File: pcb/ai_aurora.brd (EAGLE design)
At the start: 73.8 x 73.8 mm, 1 part

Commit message: schematic done
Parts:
- added BAT1, BAT2: (no value), Ai_Electromechanical:BATTERY-AAA
- added C1, C2, C3: (no value), Ai_Passives:CAP-025X050
- added D1: (no value), Ai_DiscreteSemis:TH-1N914
- added IC1: ATTINY85-DIP, Ai_IC:DIL08
- added J1: 1X02ST, Ai_Connectors:1X02-ST
- added J2: 2X03, Ai_Connectors:2X03
- added LDR: LDR-PTH, Ai_Sensors:LDR
- added Q3: (no value), Ai_DiscreteSemis:TO-92-NPN
- added Q4: (no value), Ai_DiscreteSemis:TO-92-PNP
- added R2: 1K, Ai_Passives:RES-AXIAL-0.4
- added R5: 100K, Ai_Passives:RES-AXIAL-0.4
- added R6: 10K, Ai_Passives:RES-AXIAL-0.4
- added R7: 1M, Ai_Passives:RES-AXIAL-0.4
- added U$4, U$5: LED-PL9823-F8, Ai_LED:LED-RGB-PTH
- R1: value LDR-PTH -> 1K; device Ai_Sensors:LDR -> Ai_Passives:RES-AXIAL-0.4
- moved R1 45.8 mm to (11.4, -30.5)
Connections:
- new net +: C1.1, C2.1, IC1.8, J2.2, Q4.1, R2.P$2
- new net -: C1.2, C2.2, IC1.4, J2.6, R1.P$2, R7.P$1
- new net DI: IC1.2, U$4.4
- new net DO: U$5.1
- new net GND: C3.2, J1.2, LDR.1, Q3.1, R1.P$1
- new net MISO: IC1.6, J2.1
- new net MOSI: IC1.5, J2.4
- new net N$1: BAT1.PWR@1, BAT1.PWR@2, BAT2.GND@1, BAT2.GND@2
- new net N$10: LDR.2, Q3.2, R5.P$1, R7.P$2
- new net N$12: Q3.3, R6.P$2
- new net N$13: Q4.2, R6.P$1
- new net N$2: D1.A, J1.1
- new net N$4: U$4.1, U$5.4
- new net N$6: U$4.3, U$5.3
- new net N$7: U$4.2, U$5.2
- new net RST: IC1.1, J2.5, R2.P$1
- new net SCK: IC1.7, J2.3
- new net VBAT: BAT2.PWR@1, BAT2.PWR@2, Q4.3, R5.P$2
- new net VIN: BAT1.GND@1, BAT1.GND@2, C3.1, D1.C
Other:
- board text added: "+"

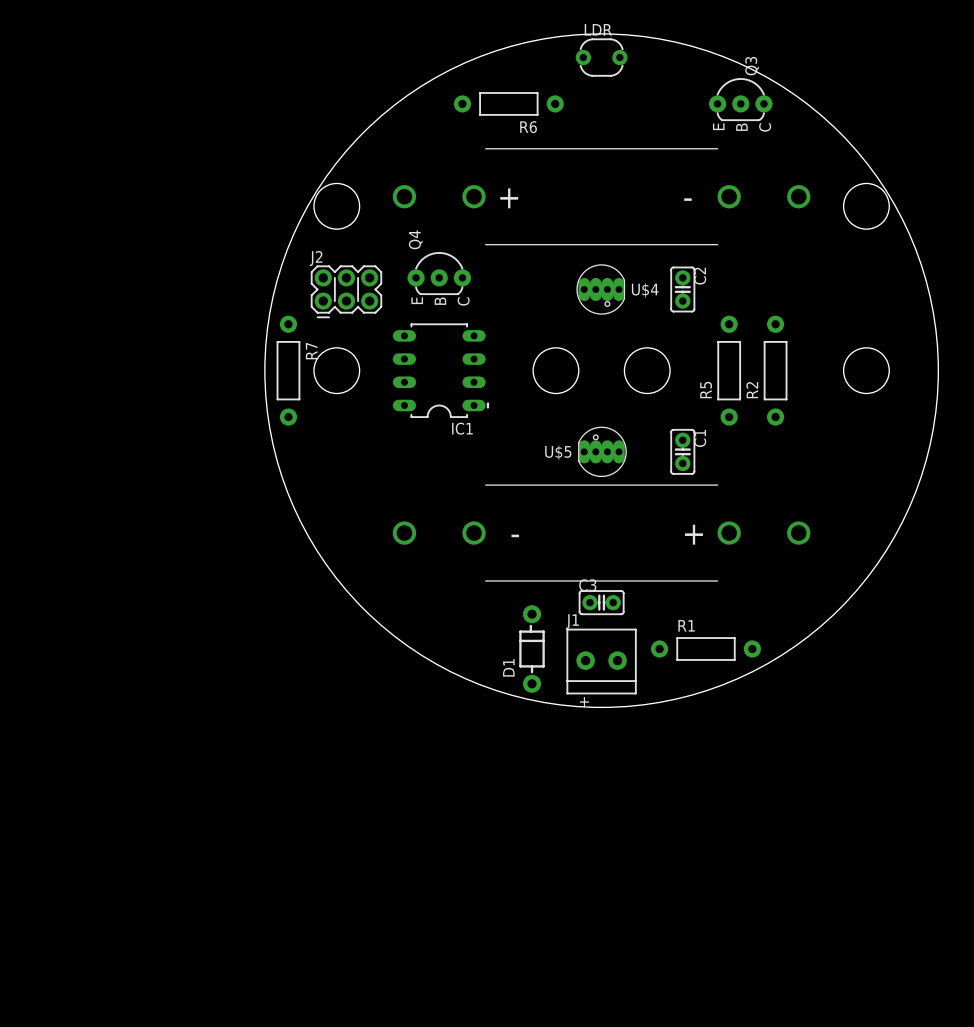
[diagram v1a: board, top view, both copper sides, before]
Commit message: some fitting issues remain
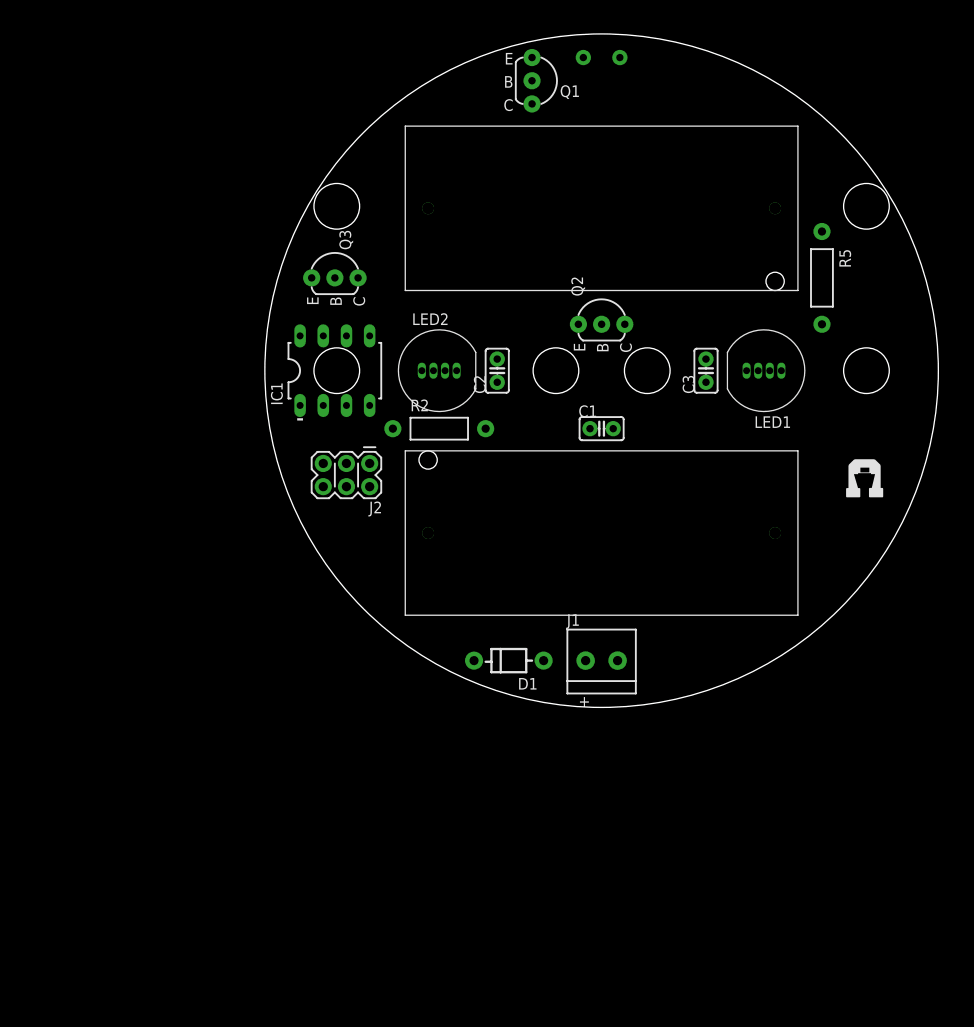
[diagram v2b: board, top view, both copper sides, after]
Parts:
- removed Q4: (no value), Ai_DiscreteSemis:TO-92-PNP
- removed R1: 1K, Ai_Passives:RES-AXIAL-0.4
- removed R6: 10K, Ai_Passives:RES-AXIAL-0.4
- removed R7: 1M, Ai_Passives:RES-AXIAL-0.4
- added LED1, LED2: LED-PL9823-F8, Ai_LED:LED-PL9823-F8
- added Q1: (no value), Ai_DiscreteSemis:TO-92-NPN
- added Q2: (no value), Ai_DiscreteSemis:TO-92-PNP
- BAT1, BAT2: device Ai_Electromechanical:BATTERY-AAA -> Ai_Electromechanical:BATTERY-CR123A
- U$4, U$5: value LED-PL9823-F8 -> AI-LOGOM; device Ai_LED:LED-RGB-PTH -> Ai_Miscellany:AI-LOGO-M
- moved Q3 48.4 mm to (-29.2, 10.2)
- moved R2 37.4 mm to (-17.8, -6.35), turned to 0 degrees
- moved U$4 35.1 mm to (26.7, -14.0)
- moved U$5 31.4 mm to (31.0, -14.0), flipped to the bottom, turned to 0 degrees
- moved C3 27.9 mm to (11.4, 0.00), turned to 90 degrees
- moved C2 22.2 mm to (-11.4, 0.00), turned to 90 degrees
- moved J2 20.3 mm to (-27.9, -11.4), turned to 180 degrees
- moved R5 14.4 mm to (24.1, 10.2), turned to 270 degrees
- moved IC1 11.4 mm to (-29.2, 0.00), turned to 0 degrees
- moved C1 9.25 mm to (0.00, -6.35), turned to 0 degrees
- moved D1 2.84 mm to (-10.2, -31.8), turned to 180 degrees
- moved BAT1 1.27 mm to (0.00, 17.8), turned to 270 degrees
- turned BAT2 to 90 degrees
- flipped LDR to the bottom
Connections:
- removed net -: C1.2, C2.2, IC1.4, J2.6, R1.P$2, R7.P$1
- removed net N$12: Q3.3, R6.P$2
- removed net N$6: U$4.3, U$5.3
- removed net N$7: U$4.2, U$5.2
- net +: now also LED1.2, LED2.2, Q2.1, Q3.1, Q3.2; no longer Q4.1
- net DI: now also LED1.1; no longer U$4.4
- net DO: now also LED2.4; no longer U$5.1
- net GND: now also C1.2, C2.2, IC1.4, J2.6, LED1.3, LED2.3, Q1.1; no longer Q3.1, R1.P$1
- net N$1: now also BAT1.+, BAT2.-; no longer BAT1.PWR@1, BAT1.PWR@2, BAT2.GND@1, BAT2.GND@2
- net N$10: now also Q1.2; no longer Q3.2, R7.P$2
- net N$13: now also Q1.3, Q2.2; no longer Q4.2, R6.P$1
- net N$4: now also LED1.4, LED2.1; no longer U$4.1, U$5.4
- net VBAT: now also BAT2.+, Q2.3, Q3.3; no longer BAT2.PWR@1, BAT2.PWR@2, Q4.3
- net VIN: now also BAT1.-; no longer BAT1.GND@1, BAT1.GND@2

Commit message: updating firmware and pcb
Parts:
- removed Q2: (no value), Ai_DiscreteSemis:TO-92-PNP
- removed Q3: (no value), Ai_DiscreteSemis:TO-92-NPN
- added JP1, JP2: 1X02-PJ, Ai_Connectors:1X02
- added R1: 10K, Ai_Passives:RES-AXIAL-0.4
- added S1, S2: SW-SPSTTH06X06, Ai_Electromechanical:SW-SPST-TH06X06
- added VR1: 1M, Ai_Passives:POT-05X05
- C3: value (none) -> 4.7uF; device Ai_Passives:CAP-025X050 -> Ai_Passives:CAP-POL-025X50
- Q1: value (none) -> FQP30N06L; device Ai_DiscreteSemis:TO-92-NPN -> Ai_DiscreteSemis:TO-220
- R2: value 1K -> 10K
- moved Q1 99.4 mm to (-52.1, -57.1), turned to 0 degrees
- moved R2 69.4 mm to (-57.1, -63.5)
- moved C3 1.27 mm to (11.4, 1.27)
- renumbered LDR to LDR1
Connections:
- net MOSI renamed MOSI/SET
- removed net MISO: IC1.6, J2.1
- removed net N$10: LDR1.2, Q1.2, R5.P$1
- removed net N$13: Q1.3, Q2.2
- removed net SCK: IC1.7, J2.3
- new net -: C1.2, C2.2, LED1.3, LED2.3, Q1.2
- new net LED_EN: IC1.3, Q1.1
- new net MISO/LDR: IC1.6, J2.1, JP1.1
- new net N$3: R1.P$2, S1.B@1
- new net N$5: R2.P$2, S2.A@1
- new net N$6: R5.P$2, VR1.2
- new net N$7: JP1.2, LDR1.2, R5.P$1
- new net SCK/BATT: IC1.7, J2.3, JP2.1
- net +: no longer IC1.8, J2.2, Q2.1, Q3.1, Q3.2, R2.P$2
- net GND: now also C3.C, Q1.3, R1.P$1, R2.P$1; no longer C1.2, C2.2, C3.2, LED1.3, LED2.3, Q1.1
- net RST: now also S1.A@1; no longer R2.P$1
- net VBAT: now also IC1.8, J2.2, JP2.2, VR1.3; no longer Q2.3, Q3.3, R5.P$2
- net VIN: now also C3.A; no longer C3.1

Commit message: updating
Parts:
- removed R5: 100K, Ai_Passives:RES-AXIAL-0.4
- added R3: 10K, Ai_Passives:RES-AXIAL-0.4
- added R4: 100K, Ai_Passives:RES-AXIAL-0.4
- R2: value 10K -> 100K
- moved R2 109.7 mm to (24.1, 10.2), turned to 270 degrees
- renumbered C3 to C11
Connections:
- net GND: now also R3.P$1, R4.P$1; no longer R2.P$1
- net LED_EN: now also R4.P$2
- net N$5: now also R3.P$2; no longer R2.P$2
- net N$6: now also R2.P$2; no longer R5.P$2
- net N$7: now also R2.P$1; no longer R5.P$1
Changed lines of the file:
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@@
 <element name="IC1" library="Ai_IC" package="DIL08" value="ATTINY85-DIP" x="-29.21" y="0"/>
 <element name="LDR1" library="Ai_Sensors" package="LDR" value="LDR-PTH" x="0" y="34.29" rot="MR0"/>
-<element name="R5" library="Ai_Passives" package="RES-AXIAL-0.4" value="100K" x="24.13" y="10.16" rot="R270"/>
+<element name="R2" library="Ai_Passives" package="RES-AXIAL-0.4" value="100K" x="24.13" y="10.16" rot="R270"/>
 <element name="BAT1" library="Ai_Electromechanical" package="BATTERY-CR123A" value="" x="0" y="17.78" rot="R270"/>
 <element name="BAT2" library="Ai_Electromechanical" package="BATTERY-CR123A" value="" x="0" y="-17.78" rot="R90"/>
@@
 <element name="J1" library="Ai_Connectors" package="1X02-ST" value="1X02ST" x="0" y="-31.75"/>
 <element name="J2" library="Ai_Connectors" package="2X03" value="2X03" x="-27.94" y="-11.43" rot="R180"/>
-<element name="C3" library="Ai_Passives" package="CAP-POL-025X50" value="4.7uF" x="11.43" y="1.27" rot="R90"/>
+<element name="C11" library="Ai_Passives" package="CAP-POL-025X50" value="4.7uF" x="11.43" y="1.27" rot="R90"/>
 <element name="LED1" library="Ai_LED" package="LED-PL9823-F8" value="LED-PL9823-F8" x="17.78" y="0" rot="R180"/>
 <element name="LED2" library="Ai_LED" package="LED-PL9823-F8" value="LED-PL9823-F8" x="-17.78" y="0"/>
@@
 <element name="Q1" library="Ai_DiscreteSemis" package="TO-220" value="FQP30N06L" x="-52.07" y="-57.15"/>
 <element name="S2" library="Ai_Electromechanical" package="SW-SPST-TH06X06" value="SW-SPSTTH06X06" x="-59.69" y="-54.61"/>
-<element name="R2" library="Ai_Passives" package="RES-AXIAL-0.4" value="10K" x="-57.15" y="-63.5"/>
+<element name="R3" library="Ai_Passives" package="RES-AXIAL-0.4" value="10K" x="-57.15" y="-63.5"/>
+<element name="R4" library="Ai_Passives" package="RES-AXIAL-0.4" value="100K" x="-57.15" y="-68.58"/>
 </elements>
 <signals>
 <signal name="GND" airwireshidden="yes">
 <contactref element="LDR1" pad="1"/>
-<contactref element="C3" pad="C"/>
+<contactref element="C11" pad="C"/>
 <contactref element="J1" pad="2"/>
 <contactref element="IC1" pad="4"/>
@@
 <contactref element="R1" pad="P$1"/>
 <contactref element="Q1" pad="3"/>
-<contactref element="R2" pad="P$1"/>
+<contactref element="R3" pad="P$1"/>
+<contactref element="R4" pad="P$1"/>
+<wire x1="-62.23" y1="-63.5" x2="-62.23" y2="-68.58" width="0" layer="19" extent="1-1"/>
 <wire x1="-49.53" y1="-57.15" x2="-62.23" y2="-63.5" width="0" layer="19" extent="1-1"/>
 <wire x1="-35.56" y1="-41.91" x2="-49.53" y2="-57.15" width="0" layer="19" extent="1-1"/>
@@
 <contactref element="D1" pad="C"/>
 <contactref element="BAT1" pad="-"/>
-<contactref element="C3" pad="A"/>
+<contactref element="C11" pad="A"/>
 <wire x1="11.43" y1="2.54" x2="-13.97" y2="-31.75" width="0" layer="19" extent="1-1"/>
 <wire x1="-19" y1="17.78" x2="11.43" y2="2.54" width="0" layer="19" extent="1-1"/>
@@
 <contactref element="IC1" pad="3"/>
 <contactref element="Q1" pad="1"/>
+<contactref element="R4" pad="P$2"/>
+<wire x1="-54.61" y1="-57.15" x2="-52.07" y2="-68.58" width="0" layer="19" extent="1-1"/>
 <wire x1="-27.94" y1="-3.81" x2="-54.61" y2="-57.15" width="0" layer="19" extent="1-1"/>
 </signal>
 <signal name="N$6">
-<contactref element="R5" pad="P$2"/>
+<contactref element="R2" pad="P$2"/>
 <contactref element="VR1" pad="2"/>
 <wire x1="24.13" y1="5.08" x2="-50.8" y2="-36.83" width="0" layer="19" extent="1-1"/>
@@
 <signal name="N$7">
 <contactref element="LDR1" pad="2"/>
-<contactref element="R5" pad="P$1"/>
+<contactref element="R2" pad="P$1"/>
 <contactref element="JP1" pad="2"/>
 <wire x1="-2" y1="34.29" x2="-49.53" y2="-46.99" width="0" layer="19" extent="1-1"/>
@@
 </signal>
 <signal name="N$5">
-<contactref element="R2" pad="P$2"/>
+<contactref element="R3" pad="P$2"/>
 <contactref element="S2" pad="A@1"/>
 <wire x1="-52.07" y1="-63.5" x2="-62.9412" y2="-56.8706" width="0" layer="19" extent="1-1"/>

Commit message: gerbers
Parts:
- removed J1: 1X02ST, Ai_Connectors:1X02-ST
- removed J2: 2X03, Ai_Connectors:2X03
- removed S1, S2: SW-SPSTTH06X06, Ai_Electromechanical:SW-SPST-TH06X06
- added ISP: 2X03, Ai_Connectors:2X03
- added M2, M3, PANEL+, PANEL-: 1X01-TERM-PANEL, Ai_Connectors:1X01-PANEL
- added RESET, SET: SW-SPSTTH06X06, Ai_Electromechanical:SW-SPST-TH06X06
- added SOLAR-IN: 1X02ST, Ai_Connectors:1X02-ST
- moved R3 89.6 mm to (-8.38, 11.7), turned to 270 degrees
- moved R4 87.3 mm to (8.38, -10.9), turned to 270 degrees
- moved VR1 74.8 mm to (-16.3, 26.9)
- moved Q1 70.1 mm to (0.00, -10.2), turned to 180 degrees
- moved JP2 48.7 mm to (-7.24, -30.2), turned to 90 degrees
- moved D1 47.1 mm to (31.8, -10.2), turned to 270 degrees
- moved LED1 44.5 mm to (-17.8, -26.7)
- moved LED2 44.5 mm to (17.8, 26.7)
- moved IC1 43.3 mm to (1.27, -30.7), turned to 270 degrees
- moved JP1 43.3 mm to (-10.9, -30.2), turned to 90 degrees
- moved C2 42.7 mm to (23.6, 24.4)
- moved U$5 40.9 mm to (0.31, 13.1), turned to 270 degrees
- moved R1 38.1 mm to (-8.38, -10.9), turned to 270 degrees
- moved R2 37.1 mm to (-8.13, 28.4), turned to 90 degrees
- moved U$4 34.8 mm to (0.31, 8.77), turned to 90 degrees
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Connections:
- removed net N$2: D1.A, J1.1
- new net VPANEL: D1.A, PANEL+.1, SOLAR-IN.1
- net GND: now also ISP.6, PANEL-.1, SOLAR-IN.2; no longer J1.2, J2.6
- net MISO/LDR: now also ISP.1; no longer J2.1
- net MOSI/SET: now also ISP.4, SET.B@1; no longer J2.4
- net N$3: now also RESET.B@1; no longer S1.B@1
- net N$5: now also SET.A@1; no longer S2.A@1
- net RST: now also ISP.5, RESET.A@1; no longer J2.5, S1.A@1
- net SCK/BATT: now also ISP.3; no longer J2.3
- net VBAT: now also ISP.2; no longer J2.2
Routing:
- net VBAT: track 0.00 -> 110.9 mm, vias 0 -> 1
- net N$7: track 0.00 -> 95.9 mm
- net +: track 0.00 -> 95.8 mm, vias 0 -> 1
- net N$4: track 0.00 -> 93.4 mm
- net -: track 0.00 -> 93.4 mm
- net VIN: track 0.00 -> 64.3 mm
- net LED_EN: track 0.00 -> 60.9 mm
- net VPANEL: track 0.00 -> 48.1 mm
- net N$1: track 0.00 -> 39.4 mm
- net MOSI/SET: track 0.00 -> 39.3 mm
- net RST: track 0.00 -> 28.5 mm
- net MISO/LDR: track 0.00 -> 28.3 mm
- net N$5: track 0.00 -> 27.9 mm
- net SCK/BATT: track 0.00 -> 22.0 mm
- net DI: track 0.00 -> 15.4 mm
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- added copper zone on layer 1, net GND
- added copper zone on layer 16, net GND
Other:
- outline, holes or cut-outs redrawn
- board text added: "AURORA"
- board text added: "Pasadena, CA"
- board text added: "SENSITIVITY"
- board text added: "The Smart Sun Jar"
- board text added: "v1.0"
- board text added: "www.acrobotic.com"

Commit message: updated libraries
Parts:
- BAT1, BAT2: value (none) -> CR123A
- C1, C2: value (none) -> 0.1uF
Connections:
- removed net +: C1.1, C2.1, LED1.2, LED2.2
- net VBAT: now also C1.1, C2.1, LED1.2, LED2.2
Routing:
- net VBAT: track 110.9 -> 208.3 mm, vias 1 -> 2
- net +: track 95.8 -> 0.00 mm, vias 1 -> 0
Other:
- outline, holes or cut-outs redrawn
- board text added: "-"
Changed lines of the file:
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@@
 <setting verticaltext="up"/>
 </settings>
-<grid distance="10" unitdist="mil" unit="mil" style="lines" multiple="1" display="yes" altdistance="0.025" altunitdist="inch" altunit="inch"/>
+<grid distance="1" unitdist="mil" unit="mil" style="lines" multiple="1" display="yes" altdistance="0.025" altunitdist="inch" altunit="inch"/>
 <layers>
 <layer number="1" name="Top" color="4" fill="1" visible="yes" active="yes"/>
@@
 <layer number="223" name="223bmp" color="24" fill="1" visible="no" active="no"/>
 <layer number="224" name="224bmp" color="25" fill="1" visible="no" active="no"/>
+<layer number="225" name="225bmp" color="7" fill="1" visible="no" active="yes"/>
+<layer number="226" name="226bmp" color="7" fill="1" visible="no" active="yes"/>
+<layer number="227" name="227bmp" color="7" fill="1" visible="no" active="yes"/>
+<layer number="228" name="228bmp" color="7" fill="1" visible="no" active="yes"/>
+<layer number="230" name="230bmp" color="7" fill="1" visible="no" active="yes"/>
 <layer number="248" name="Housing" color="7" fill="1" visible="yes" active="yes"/>
 <layer number="249" name="Edge" color="7" fill="1" visible="yes" active="yes"/>
@@
 <plain>
 <circle x="0" y="0" radius="36.875" width="0.0254" layer="20"/>
-<circle x="30.27" y="19.905" radius="2.5" width="0.0254" layer="20"/>
-<text x="36.83" y="-2.54" size="1.27" layer="21" font="vector" ratio="10" rot="R90">+</text>
+<text x="31.75" y="-2.286" size="1.778" layer="21" font="vector" ratio="10" rot="R90">+</text>
 <text x="-16.256" y="23.114" size="1.016" layer="21" font="vector" ratio="10" align="center">SENSITIVITY</text>
-<text x="2.09" y="13.845" size="1.016" layer="21" font="vector" ratio="10" rot="R90" align="center">Pasadena, CA</text>
-<text x="3.868" y="15.369" size="1.016" layer="21" font="vector" ratio="10" rot="R90" align="center">www.acrobotic.com</text>
-<text x="1.836" y="13.845" size="1.016" layer="22" font="vector" ratio="10" rot="SMR270" align="center">Pasadena, CA</text>
-<text x="3.614" y="15.369" size="1.016" layer="22" font="vector" ratio="10" rot="SMR270" align="center">www.acrobotic.com</text>
+<text x="2.1408" y="14.2006" size="1.016" layer="21" font="vector" ratio="10" rot="R90" align="center">Pasadena, CA</text>
+<text x="3.8426" y="15.8008" size="1.016" layer="21" font="vector" ratio="10" rot="R90" align="center">www.acrobotic.com</text>
+<text x="2.1408" y="13.9466" size="1.016" layer="22" font="vector" ratio="10" rot="SMR270" align="center">Pasadena, CA</text>
+<text x="3.7918" y="15.5722" size="1.016" layer="22" font="vector" ratio="10" rot="SMR270" align="center">www.acrobotic.com</text>
 <text x="-29.718" y="-18.288" size="1.016" layer="21" font="vector" ratio="10" rot="R90" align="center">v1.0</text>
 <text x="-33.274" y="0" size="2.54" layer="21" font="vector" ratio="10" rot="R90" align="center">AURORA</text>
 <text x="-29.972" y="0" size="1.778" layer="21" font="vector" ratio="10" rot="R90" align="center">The Smart Sun Jar</text>
+<text x="31.75" y="1.143" size="1.778" layer="21" font="vector" ratio="10" rot="R90">-</text>
 </plain>
 <attributes>
@@
 <attribute name="NAME" x="-9.779" y="31.115" size="1.27" layer="25" font="vector" ratio="10" rot="R90"/>
 </element>
-<element name="BAT1" library="Ai_Electromechanical" package="BATTERY-CR123A" value="" x="-19.05" y="0"/>
-<element name="BAT2" library="Ai_Electromechanical" package="BATTERY-CR123A" value="" x="19.05" y="0" rot="R180"/>
-<element name="C1" library="Ai_Passives" package="CAP-025X050" value="" x="-23.876" y="-24.384" rot="R270"/>
-<element name="C2" library="Ai_Passives" package="CAP-025X050" value="" x="23.622" y="24.384" rot="R90"/>
+<element name="BAT1" library="Ai_Electromechanical" package="BATTERY-CR123A" value="CR123A" x="-19.05" y="0"/>
+<element name="BAT2" library="Ai_Electromechanical" package="BATTERY-CR123A" value="CR123A" x="19.05" y="0" rot="R180"/>
+<element name="C1" library="Ai_Passives" package="CAP-025X050" value="0.1uF" x="-23.876" y="-24.384" rot="R270"/>
+<element name="C2" library="Ai_Passives" package="CAP-025X050" value="0.1uF" x="23.622" y="24.384" rot="R90"/>
 <element name="D1" library="Ai_DiscreteSemis" package="TH-1N914" value="" x="31.75" y="-10.16" rot="R270"/>
 <element name="SOLAR-IN" library="Ai_Connectors" package="1X02-ST" value="1X02ST" x="35.036" y="0" smashed="yes" rot="R90">
@@
 <wire x1="17.526" y1="-7.366" x2="19.05" y2="-8.89" width="0.4064" layer="1"/>
 <wire x1="19.05" y1="-8.89" x2="19.05" y2="-19" width="0.4064" layer="1"/>
-</signal>
-<signal name="+">
 <contactref element="C1" pad="1"/>
 <contactref element="C2" pad="1"/>
@@
 <wire x1="-17.272" y1="-22.86" x2="-17.145" y2="-22.733" width="0.4064" layer="1"/>
 <via x="-17.145" y="-22.733" extent="1-16" drill="0.508"/>
+<wire x1="0" y1="-6.35" x2="-0.508" y2="-6.35" width="0.4064" layer="16"/>
+<wire x1="-0.508" y1="-6.35" x2="-1.27" y2="-5.588" width="0.4064" layer="16"/>
 </signal>
 <signal name="VIN">
@@
 </signal>
 </signals>
+<errors>
+</errors>
 </board>
 </drawing>
